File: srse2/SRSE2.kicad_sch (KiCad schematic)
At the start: 84 parts, among them J1 s88-N, J2 CAN, P1 I2S, P10 PIC_SPARE, P11 RS485 TERM, P12 RS485, P13 CONN_01X03, P15 S88I, P17 RA5, P18 CONN_01X03, P19 CONN_01X02, P2 CONN_01X09, P20 O2P-Rst, P3 CONN_01X02, P4 CONN_01X04, P5 CONN_01X04, P6 ISO_I2C, P7 CAN_TERM, P8 CAN, P9 PIC_I2C, U1 Omega2, U2 ADuM1250, U3 SN65HVD230, U4 PIC18F25K80, U5 HR911105A, U6 MAX485, U7 TPS5430DDA, U8 CD4504, U9 LM317, Y1 16MHz

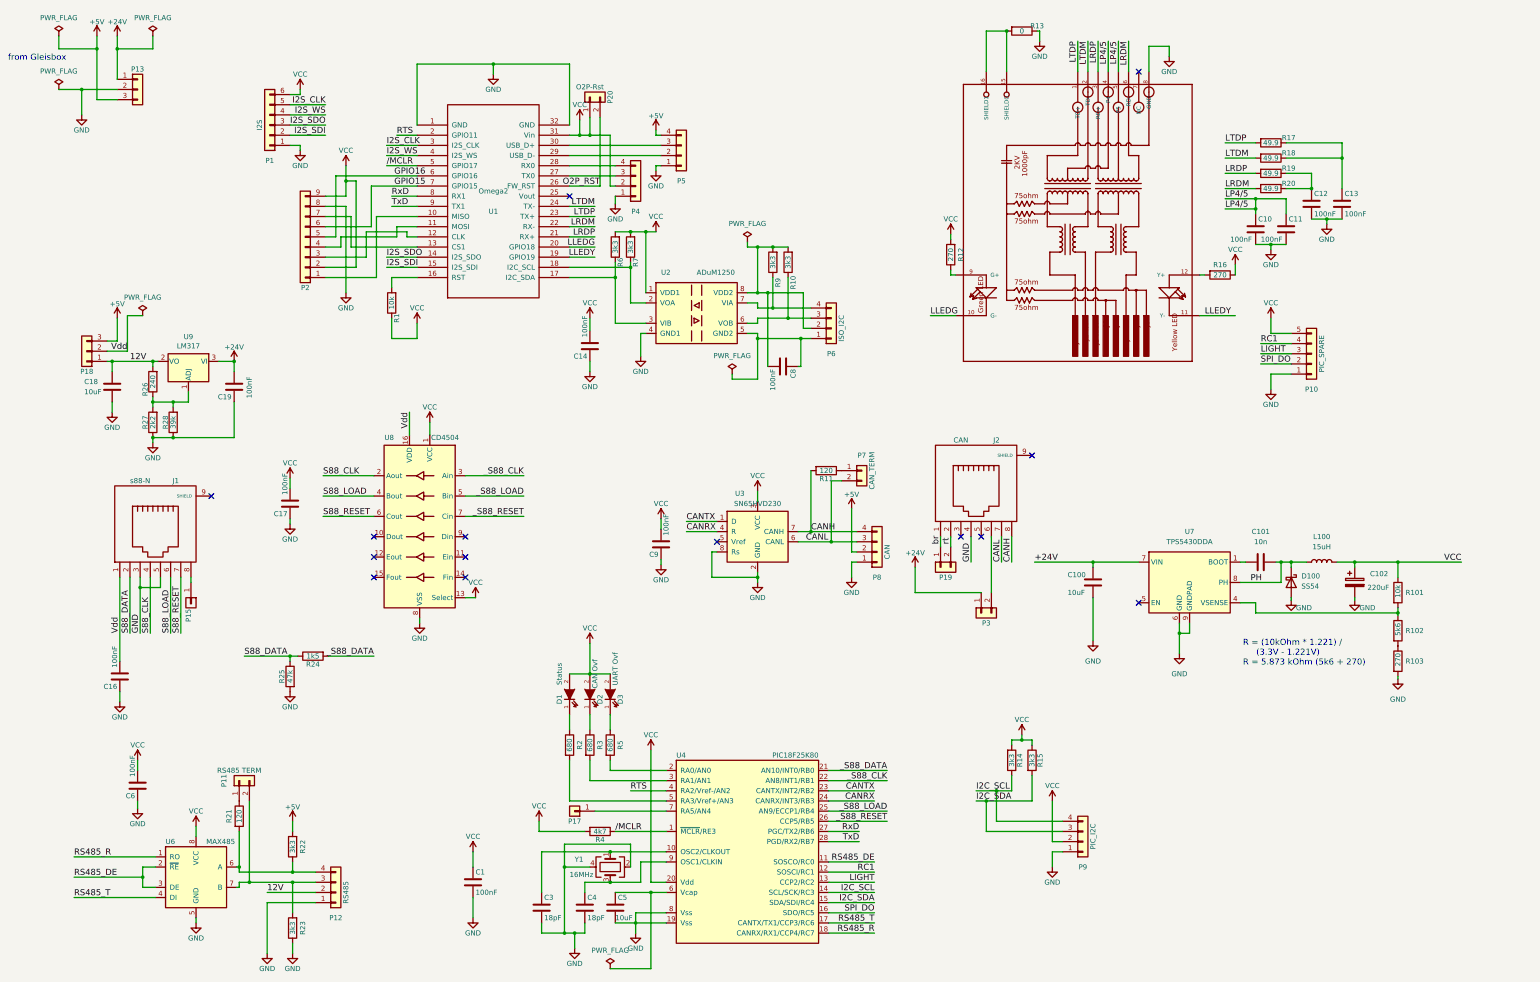
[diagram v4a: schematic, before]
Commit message: update to KiCad 7.0 - wip
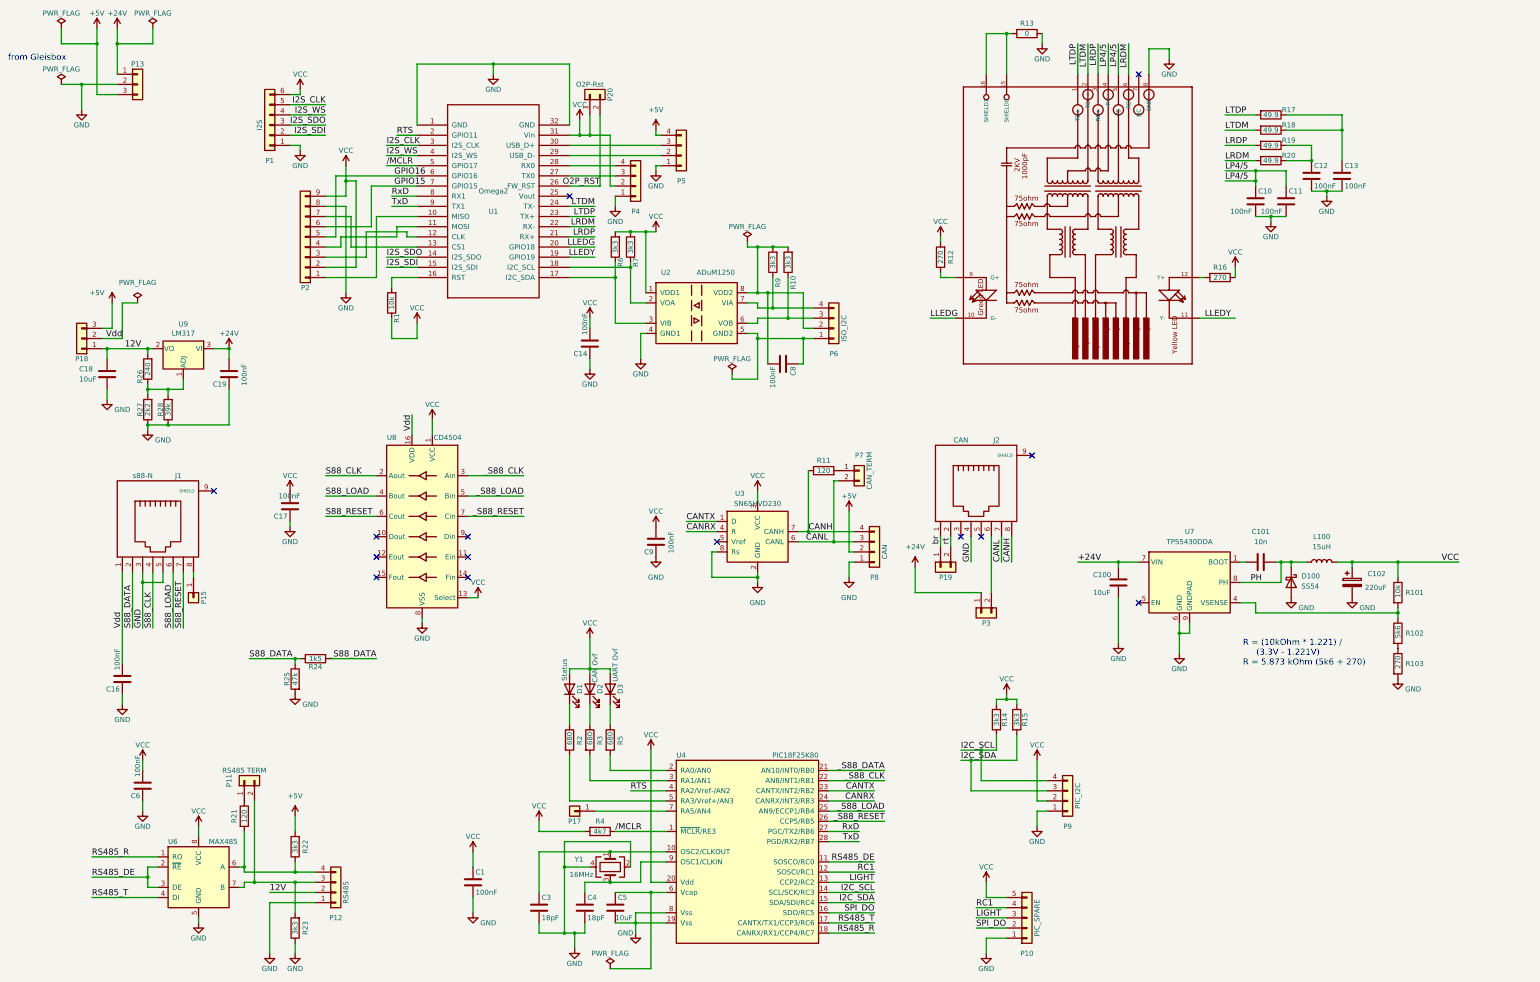
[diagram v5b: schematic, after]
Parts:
- removed D1: Status, LEDs:LED-3MM, symbol SRSE2-rescue:LED-RESCUE-SRSE2-SRSE2-rescue
- removed D2: CAN Ovf, LEDs:LED-3MM, symbol SRSE2-rescue:LED-RESCUE-SRSE2-SRSE2-rescue
- removed D3: UART Ovf, LEDs:LED-3MM, symbol SRSE2-rescue:LED-RESCUE-SRSE2-SRSE2-rescue
- removed P15: S88I, Pin_Headers:Pin_Header_Straight_1x01, symbol SRSE2-rescue:CONN_01X01-SRSE2-rescue
- removed R11: 120, Resistors_SMD:R_1206_HandSolderingII, symbol SRSE2-rescue:R-SRSE2-rescue
- removed R2, R3, R5: 680, Resistors_SMD:R_0805_HandSolderingII, symbol SRSE2-rescue:R-SRSE2-rescue
- added D1: Status, LED_THT:LED_D3.0mm, symbol Device:LED
- added D2: CAN Ovf, LED_THT:LED_D3.0mm, symbol Device:LED
- added D3: UART Ovf, LED_THT:LED_D3.0mm, symbol Device:LED
- added P15: RA5, Connector_PinHeader_2.54mm:PinHeader_1x01_P2.54mm_Vertical, symbol Connector_Generic:Conn_01x01
- added R11: 120, Resistor_SMD:R_1206_3216Metric_Pad1.30x1.75mm_HandSolder, symbol Device:R
- added R2, R3, R5: 680, Resistor_SMD:R_0805_2012Metric_Pad1.20x1.40mm_HandSolder, symbol Device:R
- C1, C8, C9: footprint Capacitors_SMD:C_0805_HandSoldering -> Capacitor_SMD:C_0805_2012Metric_Pad1.18x1.45mm_HandSolder
- C3, C4: footprint Capacitors_SMD:C_0805_HandSoldering -> Capacitor_SMD:C_0805_2012Metric
- J1, J2, P10, P11, U2, U5, U6: now left out of the parts list
- P1: footprint Pin_Headers:Pin_Header_Straight_1x06 -> Connector_PinHeader_2.54mm:PinHeader_1x06_P2.54mm_Vertical; now left out of the parts list
- P12, P4, P6, P8, P9: footprint w_conn_jst-ph:b4b-ph-kl -> Connector_JST:JST_PH_B4B-PH-K_1x04_P2.00mm_Vertical; now left out of the parts list
- P13, P18: footprint Pin_Headers:Pin_Header_Straight_1x03 -> Connector_PinHeader_2.54mm:PinHeader_1x03_P2.54mm_Vertical; now left out of the parts list
- P17: footprint Pin_Headers:Pin_Header_Straight_1x01 -> Connector_PinHeader_2.54mm:PinHeader_1x01_P2.54mm_Vertical; now left out of the parts list
- P19: footprint Pin_Headers:Pin_Header_Straight_1x02 -> Connector_PinSocket_2.54mm:PinSocket_1x02_P2.54mm_Vertical
- P2: footprint Pin_Headers:Pin_Header_Straight_1x09 -> Connector_PinHeader_2.54mm:PinHeader_1x09_P2.54mm_Vertical; now left out of the parts list
- P20: footprint Connector_PinHeader_2.54mm:PinHeader_1x02_P2.54mm_Vertical_NB -> Connector_PinHeader_2.54mm:PinHeader_1x02_P2.54mm_Vertical; now left out of the parts list
- P3: footprint Pin_Headers:Pin_Header_Straight_1x02 -> Connector_PinHeader_2.54mm:PinHeader_1x02_P2.54mm_Vertical
- P5: footprint Pin_Headers:Pin_Header_Straight_1x04 -> Connector_PinHeader_2.54mm:PinHeader_1x04_P2.54mm_Vertical; now left out of the parts list
- P7: footprint Pin_Headers:Pin_Header_Straight_1x02 -> Connector_PinSocket_2.54mm:PinSocket_1x02_P2.54mm_Vertical; now left out of the parts list
- R1, R10, R12, R14, R15, R16, R17, R18, R19, R20, R23, R26, R27, R28, R4, R6, R7, R9: footprint Resistors_SMD:R_0805_HandSolderingII -> Resistor_SMD:R_0805_2012Metric_Pad1.20x1.40mm_HandSolder
- R13: footprint Resistors_SMD:R_0805_HandSolderingII -> Resistor_SMD:R_0805_2012Metric_Pad1.20x1.40mm_HandSolder; now left out of the parts list
- R21: symbol SRSE2-rescue:R-SRSE2-rescue -> Device:R
- U4: footprint w_smd_dil:ssop-28 -> Package_SO:SSOP-28_5.3x10.2mm_P0.65mm
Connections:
- net CANH: now also R11.1
- net VCC: now also D1.2 (A), D2.2 (A), D3.2 (A)
- net at U4.2 (RA0/AN0): now also R5.2
- net at U4.3 (RA1/AN1): now also R3.2
- net at U4.5 (RA3/Vref+/AN3): now also R2.2
- net at P7.1 (Pin_1): now also R11.2
- net at J1.8: now also P15.1 (Pin_1)
- new net: D3.1 (K), R5.1
- new net: D2.1 (K), R3.1
- new net: D1.1 (K), R2.1
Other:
- moved on the sheet: C10, C100, C102, C11, C12, C13, C14, C16, C17, C18, C19, C3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

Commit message: update to KiCad 7.0 - wip
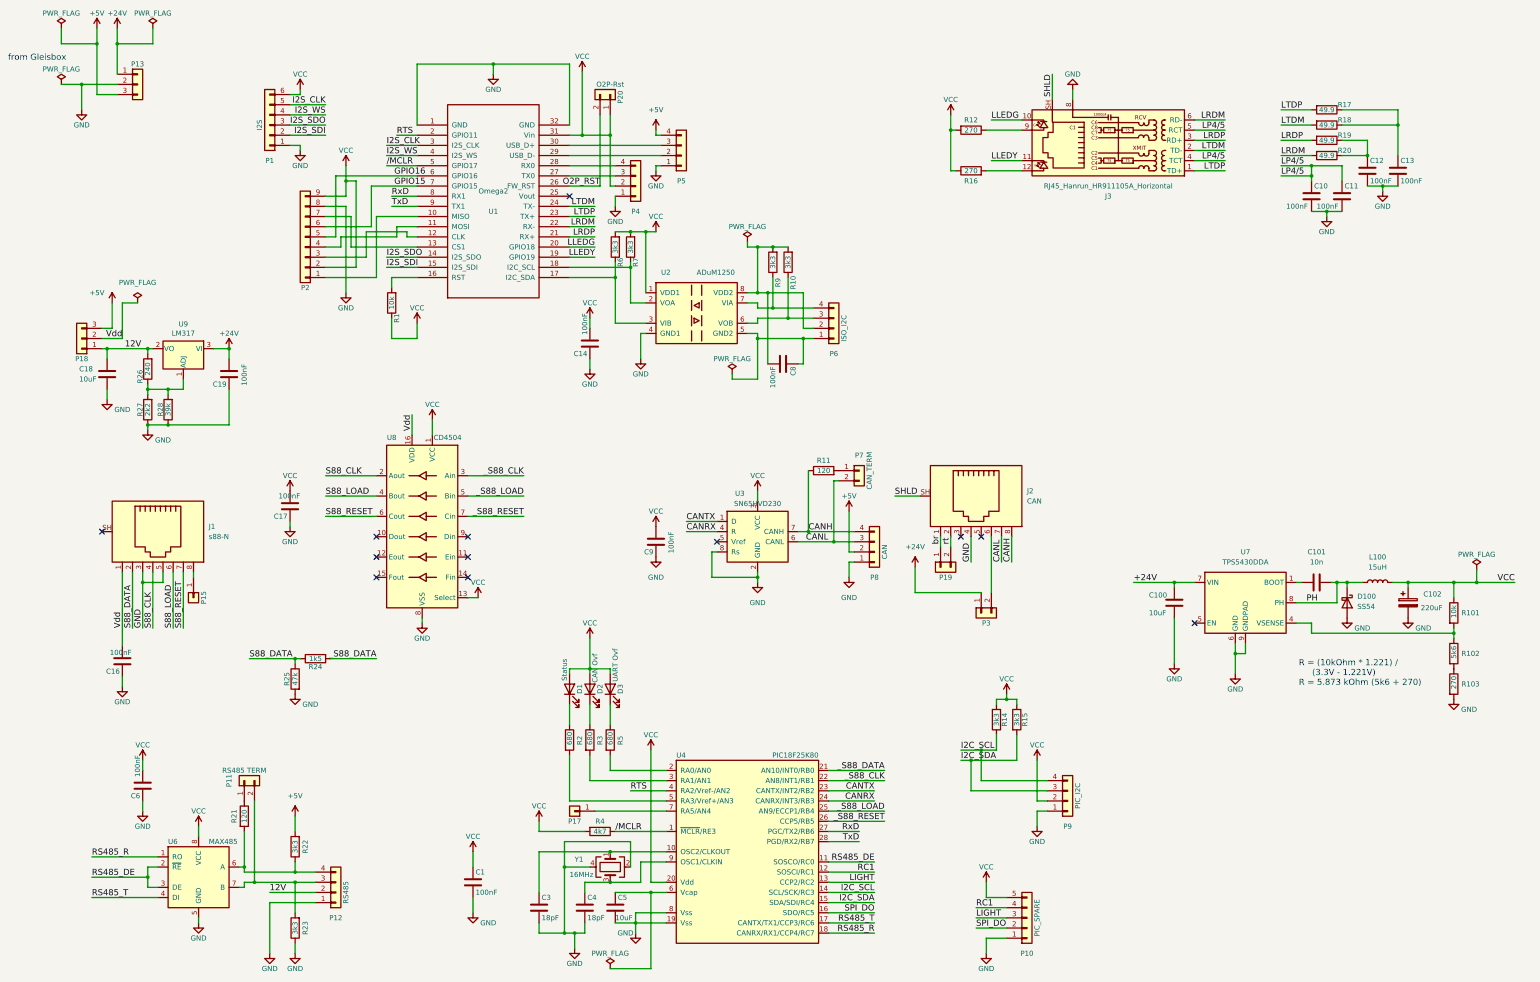
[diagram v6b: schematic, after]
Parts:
- removed J1: s88-N, w_conn_pc:megb8-8, symbol SRSE2-rescue:RJ45-SRSE2-rescue
- removed J2: CAN, w_conn_pc:megb8-8, symbol SRSE2-rescue:RJ45-SRSE2-rescue
- removed R13: 0, Resistor_SMD:R_0805_2012Metric_Pad1.20x1.40mm_HandSolder, symbol Device:R
- removed U5: HR911105A, HR911105A:RJ45ALED_1PRIMARY, symbol SRSE2-rescue:HR911105A-HR911105A
- added J1: s88-N, srse2:MEBP_8-8G, symbol Connector:RJ45_Shielded
- added J2: CAN, srse2:MEBP_8-8G, symbol Connector:RJ45_Shielded
- added J3: RJ45_Hanrun_HR911105A_Horizontal, Connector_RJ:RJ45_Hanrun_HR911105A_Horizontal, symbol Connector:RJ45_Hanrun_HR911105A_Horizontal
- C10, C11, C12, C13, C14, C16, C17, C19, C6: footprint Capacitors_SMD:C_0805_HandSoldering -> Capacitor_SMD:C_0805_2012Metric_Pad1.18x1.45mm_HandSolder
- P11: footprint Pin_Headers:Pin_Header_Straight_1x02 -> Connector_PinSocket_2.54mm:PinSocket_1x02_P2.54mm_Vertical
- R21: footprint Resistors_SMD:R_1206_HandSolderingII -> Resistor_SMD:R_1206_3216Metric_Pad1.30x1.75mm_HandSolder
- R22, R24, R25: footprint Resistors_SMD:R_0805_HandSolderingII -> Resistor_SMD:R_0805_2012Metric_Pad1.20x1.40mm_HandSolder
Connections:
- net CANH: now also J2.8
- net CANL: now also J2.7
- net GND: now also J1.3, J1.5, J2.4, J3.8
- net LLEDG: now also J3.10
- net LLEDY: now also J3.11
- net LP4/5: now also J3.4 (TCT), J3.5 (RCT)
- net LRDM: now also J3.6 (RD-)
- net LRDP: now also J3.3 (RD+)
- net LTDM: now also J3.2 (TD-)
- net LTDP: now also J3.1 (TD+)
- net S88_CLK: now also J1.4
- net S88_DATA: now also J1.2
- net S88_LOAD: now also J1.6
- net S88_RESET: now also J1.7
- net Vdd: now also J1.1
- net br: now also J2.1
- net rt: now also J2.2
- net at R16.2: now also J3.12
- net at R12.1: now also J3.9
- net at P3.2 (Pin_2): now also J2.6
- net at P15.1 (Pin_1): now also J1.8
- new net SHLD: J2.SH, J3.SH
- no-connect marks 14 -> 12
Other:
- moved on the sheet: C10, C100, C101, C102, C11, C12, C13, C16, D100, L100, P20, R101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
